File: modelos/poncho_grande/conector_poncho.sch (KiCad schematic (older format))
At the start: 1 part

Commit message: * Agregados las asociaciones con módulos desde el esquemático.
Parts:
- XA1: footprint (none) -> mod:poncho_grande
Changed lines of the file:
@@
 LIBS:conn
 LIBS:modelos_ponchos
-EELAYER 24 0
+LIBS:poncho_grande-cache
+EELAYER 25 0
 EELAYER END
 $Descr A4 11693 8268
@@
 U 1 1 560A0C4B
 P 4850 1100
-F 0 "#PWR023" H 4850 1060 30  0001 C CNN
+AR Path="/560A0C4B" Ref="#PWR023"  Part="1"
+AR Path="/560A0C15/560A0C4B" Ref="#PWR027"  Part="1"
+F 0 "#PWR027" H 4850 1060 30  0001 C CNN
 F 1 "+3.3V" H 4850 1210 30  0000 C CNN
 F 2 "" H 4850 1100 60  0000 C CNN
@@
 	5100 1500 4950 1500
 $Comp
-L GND #PWR024
+L GND #PWR028
 U 1 1 560A0C7E
 P 6750 3250
-F 0 "#PWR024" H 6750 3250 30  0001 C CNN
+F 0 "#PWR028" H 6750 3250 30  0001 C CNN
 F 1 "GND" H 6750 3180 30  0001 C CNN
 F 2 "" H 6750 3250 60  0000 C CNN
@@
 Connection ~ 6750 3100
 $Comp
-L GNDA #PWR025
+L GNDA #PWR029
 U 1 1 560A0D89
 P 6600 1800
-F 0 "#PWR025" H 6600 1800 40  0001 C CNN
+F 0 "#PWR029" H 6600 1800 40  0001 C CNN
 F 1 "GNDA" H 6600 1730 40  0000 C CNN
 F 2 "" H 6600 1800 60  0000 C CNN
@@
 	6500 1200 6500 1050
 $Comp
-L +5V #PWR026
+L +5V #PWR030
 U 1 1 560A0FA4
 P 6500 1050
-F 0 "#PWR026" H 6500 1140 20  0001 C CNN
+F 0 "#PWR030" H 6500 1140 20  0001 C CNN
 F 1 "+5V" H 6500 1140 30  0000 C CNN
 F 2 "" H 6500 1050 60  0000 C CNN
@@
 $EndComp
 $Comp
-L GND #PWR027
+L GND #PWR031
 U 1 1 560A117F
 P 4750 6000
-F 0 "#PWR027" H 4750 6000 30  0001 C CNN
+F 0 "#PWR031" H 4750 6000 30  0001 C CNN
 F 1 "GND" H 4750 5930 30  0001 C CNN
 F 2 "" H 4750 6000 60  0000 C CNN
@@
 Connection ~ 4750 5750
 $Comp
-L +3.3VP #PWR028
+L +3.3VP #PWR032
 U 1 1 560A13F3
 P 4750 3900
-F 0 "#PWR028" H 4800 3930 20  0001 C CNN
+F 0 "#PWR032" H 4800 3930 20  0001 C CNN
 F 1 "+3.3VP" H 4750 3990 30  0000 C CNN
 F 2 "" H 4750 3900 60  0000 C CNN
@@
 $EndComp
 $Comp
-L +5P #PWR32
+L +5P #PWR033
 U 1 1 560A1407
 P 6400 3900
-F 0 "#PWR32" H 6400 4030 20  0001 C CNN
+F 0 "#PWR033" H 6400 4030 20  0001 C CNN
 F 1 "+5P" H 6400 4000 30  0000 C CNN
 F 2 "" H 6400 3900 60  0000 C CNN
@@
 	5100 3100 3250 3100
 $Comp
-L GNDA #PWR029
+L GNDA #PWR034
 U 1 1 560A1A14
 P 4850 1500
-F 0 "#PWR029" H 4850 1500 40  0001 C CNN
+F 0 "#PWR034" H 4850 1500 40  0001 C CNN
 F 1 "GNDA" H 4850 1430 40  0000 C CNN
 F 2 "" H 4850 1500 60  0000 C CNN
@@
 DAC
 $Comp
-L +3.3VADC #PWR030
+L +3.3VADC #PWR035
 U 1 1 560A1ACD
 P 4650 2050
-F 0 "#PWR030" H 4650 2170 20  0001 C CNN
+F 0 "#PWR035" H 4650 2170 20  0001 C CNN
 F 1 "+3.3VADC" H 4650 2140 30  0000 C CNN
 F 2 "" H 4650 2050 60  0000 C CNN
@@
 F 0 "XA1" H 5650 1900 60  0000 C CNN
 F 1 "Poncho" H 5700 -200 60  0000 C CNN
-F 2 "" H 5350 1500 60  0000 C CNN
+F 2 "mod:poncho_grande" H 5750 -300 60  0000 C CNN
 F 3 "" H 5350 1500 60  0000 C CNN
 	1    5350 1500
@@
 F 0 "XA1" H 5650 4650 60  0000 C CNN
 F 1 "Poncho" H 5700 2550 60  0000 C CNN
-F 2 "" H 5350 4250 60  0000 C CNN
+F 2 "mod:poncho_grande" H 5350 4250 60  0001 C CNN
 F 3 "" H 5350 4250 60  0000 C CNN
 	2    5350 4250
@@
 WAKEUP
 $Comp
-L PWR_FLAG #FLG031
+L PWR_FLAG #FLG036
 U 1 1 560A61E2
 P 6750 1100
-F 0 "#FLG031" H 6750 1195 30  0001 C CNN
+F 0 "#FLG036" H 6750 1195 30  0001 C CNN
 F 1 "PWR_FLAG" H 6750 1280 30  0000 C CNN
 F 2 "" H 6750 1100 60  0000 C CNN
@@
 $EndComp
 $Comp
-L PWR_FLAG #FLG032
+L PWR_FLAG #FLG037
 U 1 1 560A61F6
 P 6550 1650
-F 0 "#FLG032" H 6550 1745 30  0001 C CNN
+F 0 "#FLG037" H 6550 1745 30  0001 C CNN
 F 1 "PWR_FLAG" H 6550 1830 30  0000 C CNN
 F 2 "" H 6550 1650 60  0000 C CNN

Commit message: * Mejoras y emprolijamiento en el esquemático y el PCB.
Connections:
- net labels added: +5VP
- net labels removed: +5P
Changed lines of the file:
@@
 EESchema Schematic File Version 2
-LIBS:power
 LIBS:modelos_ponchos
-LIBS:conn
+LIBS:misc
+LIBS:poncho_grande-cache
 EELAYER 25 0
 EELAYER END
@@
 $EndDescr
 $Comp
-L +3.3V #PWR30
+L +3.3V #PWR027
 U 1 1 560A0C4B
 P 4850 1100
-F 0 "#PWR30" H 4850 1060 30  0001 C CNN
+F 0 "#PWR027" H 4850 1060 30  0001 C CNN
 F 1 "+3.3V" H 4850 1210 30  0000 C CNN
 F 2 "" H 4850 1100 60  0000 C CNN
@@
 	5100 1500 4950 1500
 $Comp
-L GND #PWR35
+L GND #PWR028
 U 1 1 560A0C7E
 P 6750 3250
-F 0 "#PWR35" H 6750 3250 30  0001 C CNN
+F 0 "#PWR028" H 6750 3250 30  0001 C CNN
 F 1 "GND" H 6750 3180 30  0001 C CNN
 F 2 "" H 6750 3250 60  0000 C CNN
@@
 Connection ~ 6750 3100
 $Comp
-L GNDA #PWR34
+L GNDA #PWR029
 U 1 1 560A0D89
 P 6600 1800
-F 0 "#PWR34" H 6600 1800 40  0001 C CNN
+F 0 "#PWR029" H 6600 1800 40  0001 C CNN
 F 1 "GNDA" H 6600 1730 40  0000 C CNN
 F 2 "" H 6600 1800 60  0000 C CNN
@@
 	6600 1750 6450 1750
 Connection ~ 6450 1750
-Wire Wire Line
-	6300 1200 6500 1200
-Wire Wire Line
-	6500 1200 6500 1050
-$Comp
-L +5V #PWR33
-U 1 1 560A0FA4
-P 6500 1050
-F 0 "#PWR33" H 6500 1140 20  0001 C CNN
-F 1 "+5V" H 6500 1140 30  0000 C CNN
-F 2 "" H 6500 1050 60  0000 C CNN
-F 3 "" H 6500 1050 60  0000 C CNN
-	1    6500 1050
-	1    0    0    -1
-$EndComp
-$Comp
-L GND #PWR29
+$Comp
+L GND #PWR030
 U 1 1 560A117F
 P 4750 6000
-F 0 "#PWR29" H 4750 6000 30  0001 C CNN
+F 0 "#PWR030" H 4750 6000 30  0001 C CNN
 F 1 "GND" H 4750 5930 30  0001 C CNN
 F 2 "" H 4750 6000 60  0000 C CNN
@@
 Connection ~ 4750 5750
 $Comp
-L +3.3VP #PWR28
+L +3.3VP #PWR031
 U 1 1 560A13F3
 P 4750 3900
-F 0 "#PWR28" H 4800 3930 20  0001 C CNN
+F 0 "#PWR031" H 4800 3930 20  0001 C CNN
 F 1 "+3.3VP" H 4750 3990 30  0000 C CNN
 F 2 "" H 4750 3900 60  0000 C CNN
@@
 	1    0    0    -1
 $EndComp
-$Comp
-L +5P #PWR32
-U 1 1 560A1407
-P 6400 3900
-F 0 "#PWR32" H 6400 4030 20  0001 C CNN
-F 1 "+5P" H 6400 4000 30  0000 C CNN
-F 2 "" H 6400 3900 60  0000 C CNN
-F 3 "" H 6400 3900 60  0000 C CNN
-	1    6400 3900
-	1    0    0    -1
-$EndComp
-Wire Wire Line
-	6300 3950 6400 3950
-Wire Wire Line
-	6400 3950 6400 3900
 Wire Wire Line
 	5100 3950 4750 3950
@@
 	5100 3100 3250 3100
 $Comp
-L GNDA #PWR31
+L GNDA #PWR032
 U 1 1 560A1A14
 P 4850 1500
-F 0 "#PWR31" H 4850 1500 40  0001 C CNN
+F 0 "#PWR032" H 4850 1500 40  0001 C CNN
 F 1 "GNDA" H 4850 1430 40  0000 C CNN
 F 2 "" H 4850 1500 60  0000 C CNN
@@
 DAC
 $Comp
-L +3.3VADC #PWR27
+L +3.3VADC #PWR033
 U 1 1 560A1ACD
 P 4650 2050
-F 0 "#PWR27" H 4650 2170 20  0001 C CNN
+F 0 "#PWR033" H 4650 2170 20  0001 C CNN
 F 1 "+3.3VADC" H 4650 2140 30  0000 C CNN
 F 2 "" H 4650 2050 60  0000 C CNN
@@
 Wire Wire Line
 	6300 5350 6850 5350
-Wire Wire Line
-	6300 5450 7500 5450
 Wire Wire Line
 	6300 5550 7500 5550
@@
 WAKEUP
 $Comp
-L PWR_FLAG #FLG2
+L PWR_FLAG #FLG034
 U 1 1 560A61E2
 P 6750 1100
-F 0 "#FLG2" H 6750 1195 30  0001 C CNN
+F 0 "#FLG034" H 6750 1195 30  0001 C CNN
 F 1 "PWR_FLAG" H 6750 1280 30  0000 C CNN
 F 2 "" H 6750 1100 60  0000 C CNN
@@
 $EndComp
 $Comp
-L PWR_FLAG #FLG1
+L PWR_FLAG #FLG035
 U 1 1 560A61F6
 P 6550 1650
-F 0 "#FLG1" H 6550 1745 30  0001 C CNN
+F 0 "#FLG035" H 6550 1745 30  0001 C CNN
 F 1 "PWR_FLAG" H 6550 1830 30  0000 C CNN
 F 2 "" H 6550 1650 60  0000 C CNN
@@
 	6550 1650 6450 1650
 Connection ~ 6450 1650
+Wire Wire Line
+	6300 5450 7500 5450
+Wire Wire Line
+	6450 1050 6450 1200
+Wire Wire Line
+	6450 1200 6300 1200
+$Comp
+L +5V #PWR036
+U 1 1 560C551F
+P 6450 1050
+F 0 "#PWR036" H 6450 1140 20  0001 C CNN
+F 1 "+5V" H 6450 1140 30  0000 C CNN
+F 2 "" H 6450 1050 60  0000 C CNN
+F 3 "" H 6450 1050 60  0000 C CNN
+	1    6450 1050
+	1    0    0    -1
+$EndComp
+Wire Wire Line
+	6550 3800 6550 3950
+Wire Wire Line
+	6550 3950 6300 3950
+$Comp
+L +5VP #PWR037
+U 1 1 560CBF57
+P 6550 3800
+F 0 "#PWR037" H 6550 3890 20  0001 C CNN
+F 1 "+5VP" H 6550 3890 30  0000 C CNN
+F 2 "" H 6550 3800 60  0000 C CNN
+F 3 "" H 6550 3800 60  0000 C CNN
+	1    6550 3800
+	1    0    0    -1
+$EndComp
 $EndSCHEMATC

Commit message: * Cambio el conector de poncho por un cambio de nombre en la biblioteca.
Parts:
- removed XA1: Poncho, mod:poncho_grande, symbol Poncho
- added XA1: Conn_Poncho2P_2x_20x2, symbol Conn_Poncho2P_2x_20x2
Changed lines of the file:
@@
 LIBS:modelos_ponchos
 LIBS:misc
-LIBS:poncho_grande-cache
 EELAYER 25 0
 EELAYER END
@@
 Text HLabel 7500 5850 2    60   BiDi ~ 0
 GPIO8
-$Comp
-L Poncho XA1
-U 1 1 560A30D2
-P 5350 1500
-F 0 "XA1" H 5650 1900 60  0000 C CNN
-F 1 "Poncho" H 5700 -200 60  0000 C CNN
-F 2 "mod:poncho_grande" H 5750 -300 60  0000 C CNN
-F 3 "" H 5350 1500 60  0000 C CNN
-	1    5350 1500
-	1    0    0    -1
-$EndComp
-$Comp
-L Poncho XA1
-U 2 1 560A30E6
-P 5350 4250
-F 0 "XA1" H 5650 4650 60  0000 C CNN
-F 1 "Poncho" H 5700 2550 60  0000 C CNN
-F 2 "mod:poncho_grande" H 5350 4250 60  0001 C CNN
-F 3 "" H 5350 4250 60  0000 C CNN
-	2    5350 4250
-	1    0    0    -1
-$EndComp
 Wire Wire Line
 	6300 1400 6950 1400
@@
 	1    0    0    -1
 $EndComp
+$Comp
+L Conn_Poncho2P_2x_20x2 XA1
+U 2 1 560C5732
+P 5350 4250
+F 0 "XA1" H 5650 4650 60  0000 C CNN
+F 1 "Conn_Poncho2P_2x_20x2" H 5700 2550 60  0000 C CNN
+F 2 "" H 5350 4250 60  0000 C CNN
+F 3 "" H 5350 4250 60  0000 C CNN
+	2    5350 4250
+	1    0    0    -1
+$EndComp
+$Comp
+L Conn_Poncho2P_2x_20x2 XA1
+U 1 1 560C57B9
+P 5350 1500
+F 0 "XA1" H 5650 1900 60  0000 C CNN
+F 1 "Conn_Poncho2P_2x_20x2" H 5700 -200 60  0000 C CNN
+F 2 "mod:poncho_grande" H 5650 -300 60  0000 C CNN
+F 3 "" H 5350 1500 60  0000 C CNN
+	1    5350 1500
+	1    0    0    -1
+$EndComp

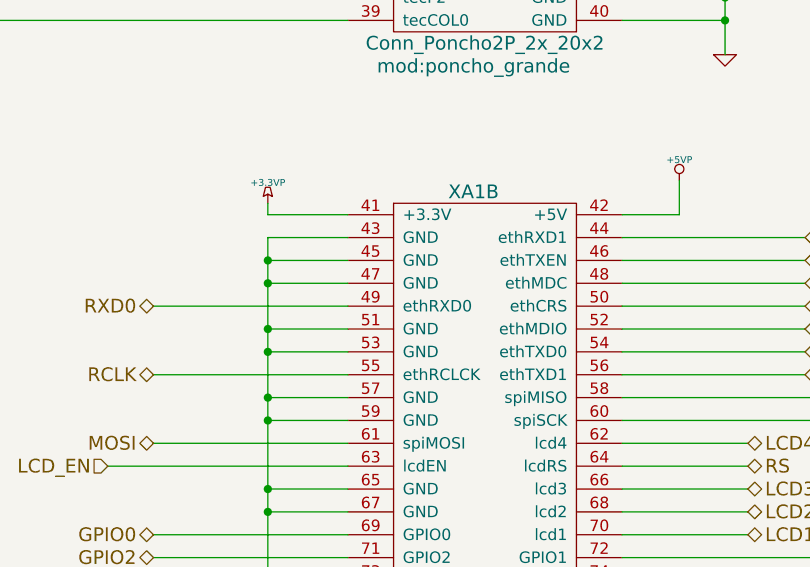
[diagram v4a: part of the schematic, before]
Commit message: * Cambios en el esquemático. Ejemplo de Poncho simple con área para prototipado.
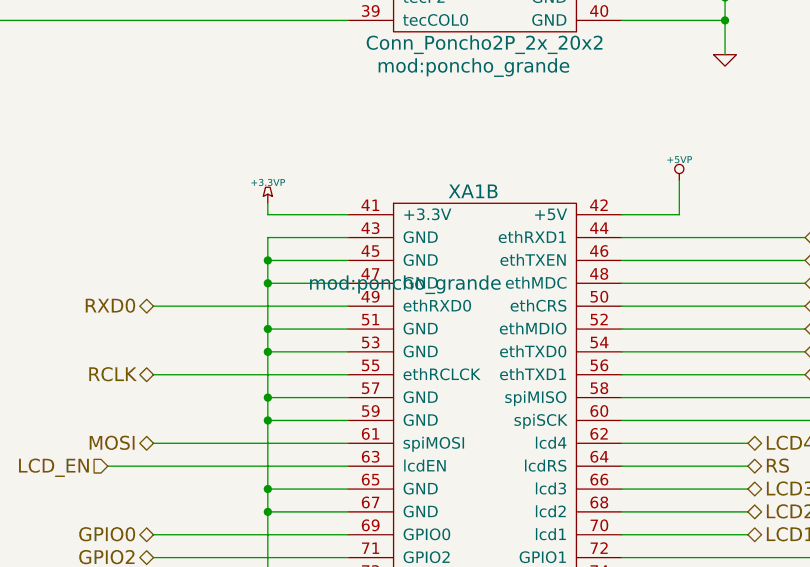
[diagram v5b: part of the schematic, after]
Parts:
- XA1: footprint (none) -> mod:poncho_grande
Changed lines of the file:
@@
 LIBS:modelos_ponchos
 LIBS:misc
+LIBS:conn
+LIBS:poncho_grande-cache
 EELAYER 25 0
 EELAYER END
@@
 $EndDescr
 $Comp
-L +3.3V #PWR027
+L +3.3V #PWR013
 U 1 1 560A0C4B
 P 4850 1100
-F 0 "#PWR027" H 4850 1060 30  0001 C CNN
+F 0 "#PWR013" H 4850 1060 30  0001 C CNN
 F 1 "+3.3V" H 4850 1210 30  0000 C CNN
 F 2 "" H 4850 1100 60  0000 C CNN
@@
 	5100 1500 4950 1500
 $Comp
-L GND #PWR028
+L GND #PWR014
 U 1 1 560A0C7E
 P 6750 3250
-F 0 "#PWR028" H 6750 3250 30  0001 C CNN
+F 0 "#PWR014" H 6750 3250 30  0001 C CNN
 F 1 "GND" H 6750 3180 30  0001 C CNN
 F 2 "" H 6750 3250 60  0000 C CNN
@@
 Connection ~ 6750 3100
 $Comp
-L GNDA #PWR029
+L GNDA #PWR015
 U 1 1 560A0D89
 P 6600 1800
-F 0 "#PWR029" H 6600 1800 40  0001 C CNN
+F 0 "#PWR015" H 6600 1800 40  0001 C CNN
 F 1 "GNDA" H 6600 1730 40  0000 C CNN
 F 2 "" H 6600 1800 60  0000 C CNN
@@
 Connection ~ 6450 1750
 $Comp
-L GND #PWR030
+L GND #PWR016
 U 1 1 560A117F
 P 4750 6000
-F 0 "#PWR030" H 4750 6000 30  0001 C CNN
+F 0 "#PWR016" H 4750 6000 30  0001 C CNN
 F 1 "GND" H 4750 5930 30  0001 C CNN
 F 2 "" H 4750 6000 60  0000 C CNN
@@
 Connection ~ 4750 5750
 $Comp
-L +3.3VP #PWR031
+L +3.3VP #PWR017
 U 1 1 560A13F3
 P 4750 3900
-F 0 "#PWR031" H 4800 3930 20  0001 C CNN
+F 0 "#PWR017" H 4800 3930 20  0001 C CNN
 F 1 "+3.3VP" H 4750 3990 30  0000 C CNN
 F 2 "" H 4750 3900 60  0000 C CNN
@@
 	5100 3100 3250 3100
 $Comp
-L GNDA #PWR032
+L GNDA #PWR018
 U 1 1 560A1A14
 P 4850 1500
-F 0 "#PWR032" H 4850 1500 40  0001 C CNN
+F 0 "#PWR018" H 4850 1500 40  0001 C CNN
 F 1 "GNDA" H 4850 1430 40  0000 C CNN
 F 2 "" H 4850 1500 60  0000 C CNN
@@
 DAC
 $Comp
-L +3.3VADC #PWR033
+L +3.3VADC #PWR019
 U 1 1 560A1ACD
 P 4650 2050
-F 0 "#PWR033" H 4650 2170 20  0001 C CNN
+F 0 "#PWR019" H 4650 2170 20  0001 C CNN
 F 1 "+3.3VADC" H 4650 2140 30  0000 C CNN
 F 2 "" H 4650 2050 60  0000 C CNN
@@
 WAKEUP
 $Comp
-L PWR_FLAG #FLG034
+L PWR_FLAG #FLG020
 U 1 1 560A61E2
 P 6750 1100
-F 0 "#FLG034" H 6750 1195 30  0001 C CNN
+F 0 "#FLG020" H 6750 1195 30  0001 C CNN
 F 1 "PWR_FLAG" H 6750 1280 30  0000 C CNN
 F 2 "" H 6750 1100 60  0000 C CNN
@@
 $EndComp
 $Comp
-L PWR_FLAG #FLG035
+L PWR_FLAG #FLG021
 U 1 1 560A61F6
 P 6550 1650
-F 0 "#FLG035" H 6550 1745 30  0001 C CNN
+F 0 "#FLG021" H 6550 1745 30  0001 C CNN
 F 1 "PWR_FLAG" H 6550 1830 30  0000 C CNN
 F 2 "" H 6550 1650 60  0000 C CNN
@@
 	6450 1200 6300 1200
 $Comp
-L +5V #PWR036
+L +5V #PWR022
 U 1 1 560C551F
 P 6450 1050
-F 0 "#PWR036" H 6450 1140 20  0001 C CNN
+F 0 "#PWR022" H 6450 1140 20  0001 C CNN
 F 1 "+5V" H 6450 1140 30  0000 C CNN
 F 2 "" H 6450 1050 60  0000 C CNN
@@
 	6550 3950 6300 3950
 $Comp
-L +5VP #PWR037
+L +5VP #PWR023
 U 1 1 560CBF57
 P 6550 3800
-F 0 "#PWR037" H 6550 3890 20  0001 C CNN
+F 0 "#PWR023" H 6550 3890 20  0001 C CNN
 F 1 "+5VP" H 6550 3890 30  0000 C CNN
 F 2 "" H 6550 3800 60  0000 C CNN
@@
 F 0 "XA1" H 5650 4650 60  0000 C CNN
 F 1 "Conn_Poncho2P_2x_20x2" H 5700 2550 60  0000 C CNN
-F 2 "" H 5350 4250 60  0000 C CNN
+F 2 "mod:poncho_grande" H 5350 4250 60  0000 C CNN
 F 3 "" H 5350 4250 60  0000 C CNN
 	2    5350 4250

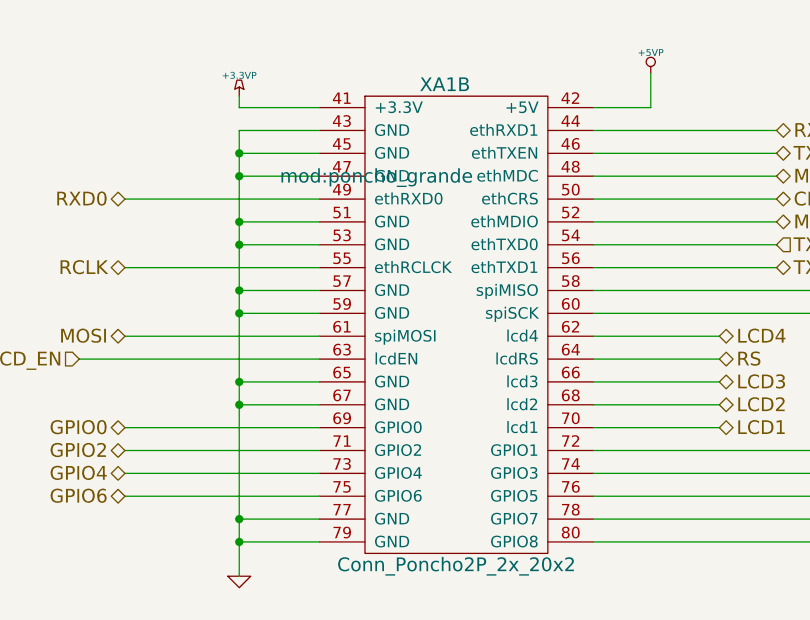
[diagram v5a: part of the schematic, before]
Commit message: * Actualizado el modelo de Poncho Grande. Ya terminado de rutear.
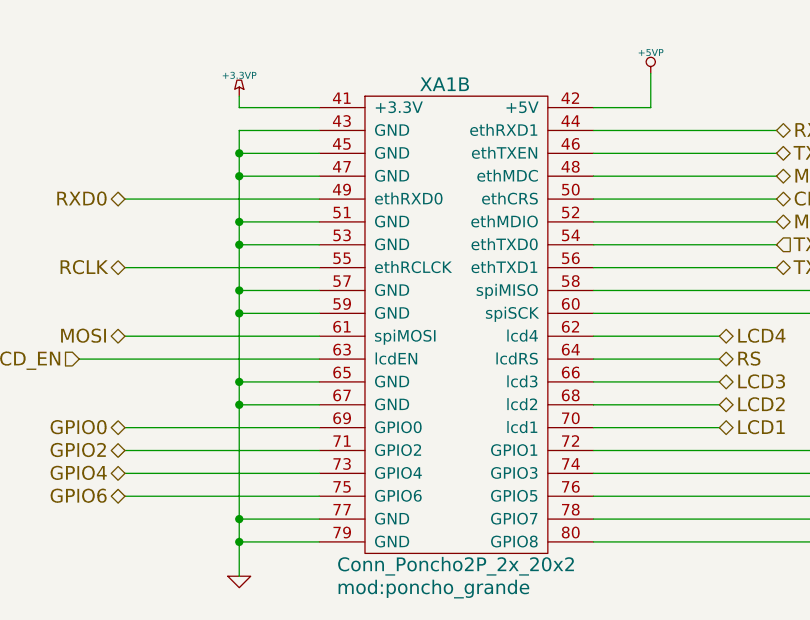
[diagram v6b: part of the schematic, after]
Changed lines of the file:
@@
 EESchema Schematic File Version 2
-LIBS:modelos_ponchos
-LIBS:misc
-LIBS:conn
+LIBS:Poncho_Esqueleto
+LIBS:Misc_Poncho_Grande
 LIBS:poncho_grande-cache
 EELAYER 25 0
@@
 F 0 "XA1" H 5650 4650 60  0000 C CNN
 F 1 "Conn_Poncho2P_2x_20x2" H 5700 2550 60  0000 C CNN
-F 2 "mod:poncho_grande" H 5350 4250 60  0000 C CNN
+F 2 "mod:poncho_grande" H 5600 2450 60  0000 C CNN
 F 3 "" H 5350 4250 60  0000 C CNN
 	2    5350 4250
